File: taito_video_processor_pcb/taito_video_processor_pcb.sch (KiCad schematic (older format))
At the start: 342 parts, among them J1 14pin, J19 2pin, J2 14pin, J3 50pin, J6 50pin, Q1 2N3904, Q2 2N3904, Q3 2N3904, Q4 2N3904, Q5 2N3904, Q6 2N3904, Q7 2N3904, Q8 2N3905, SW1 SW_Push, U1 245_1, U10 4116, U100 LS00, U101 LS08, U102 LS10, U103 LS00, U104 157_1, U105 299_1, U106 299_1, U107 299_1, U108 299_1, U109 299_1, U11 4116, U110 299_1, U12 4116, U13 4116, U14 4116, U15 4116, U16 4116, U17 4116, U18 68A45, U19 86_2, U2 245_1, U20 86_1, U21 157_1, U22 LS32, U23 161_1, U24 LS04, U25 374_1, U26 4116, U27 4116, U28 4116, U29 4116, U3 2114, U30 4116, U31 4116, U32 4116, U33 4116, U34 LS374, U35 153_1, U36 LS74, U37 LS08, U38 74S113, U39 LS04, U4 2114, U40 7417, U41 4116, U42 4116, U43 4116, U44 4116, U45 4116, U46 4116, U47 4116, U48 4116, U49 LS32, U5 157_1, U50 86_3, U51 LS86, U52 153_1, U53 153_1, U54 153_1, U55 157_1, U56 2148_1, U57 2148_2, U58 7417, U59 4116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

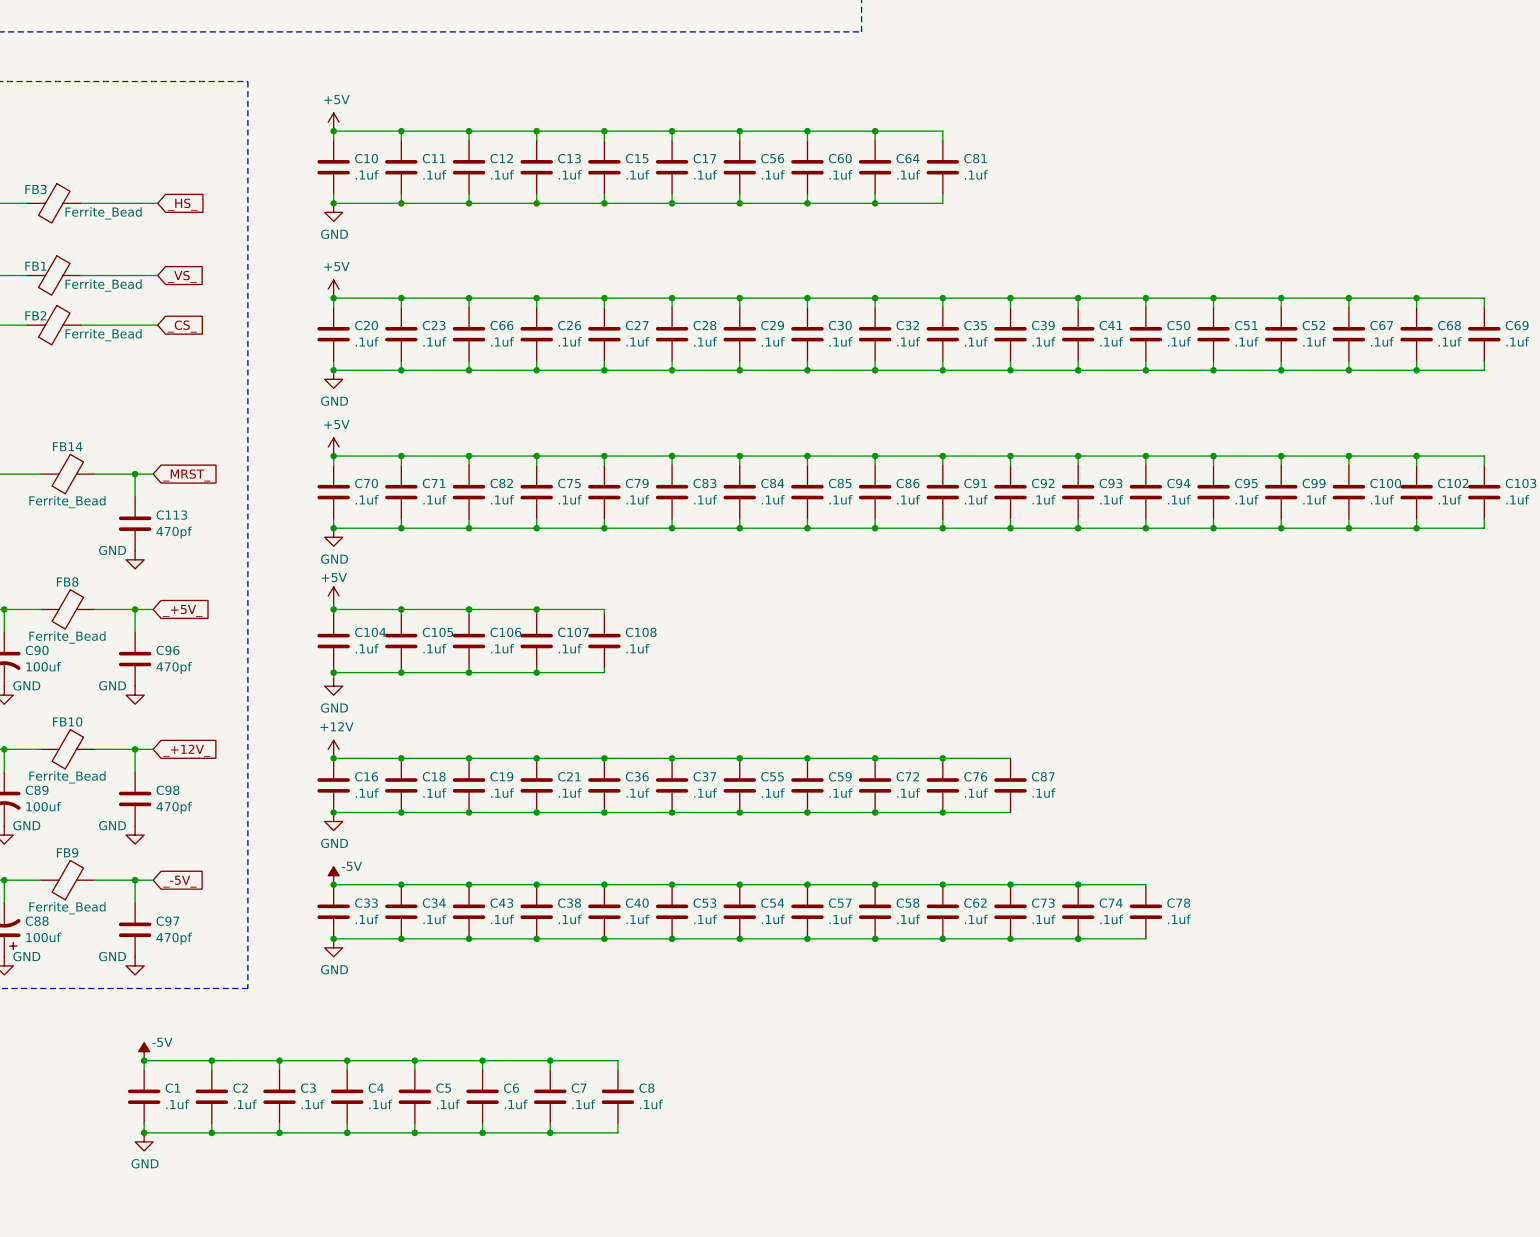
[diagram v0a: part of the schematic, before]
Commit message: Added traces
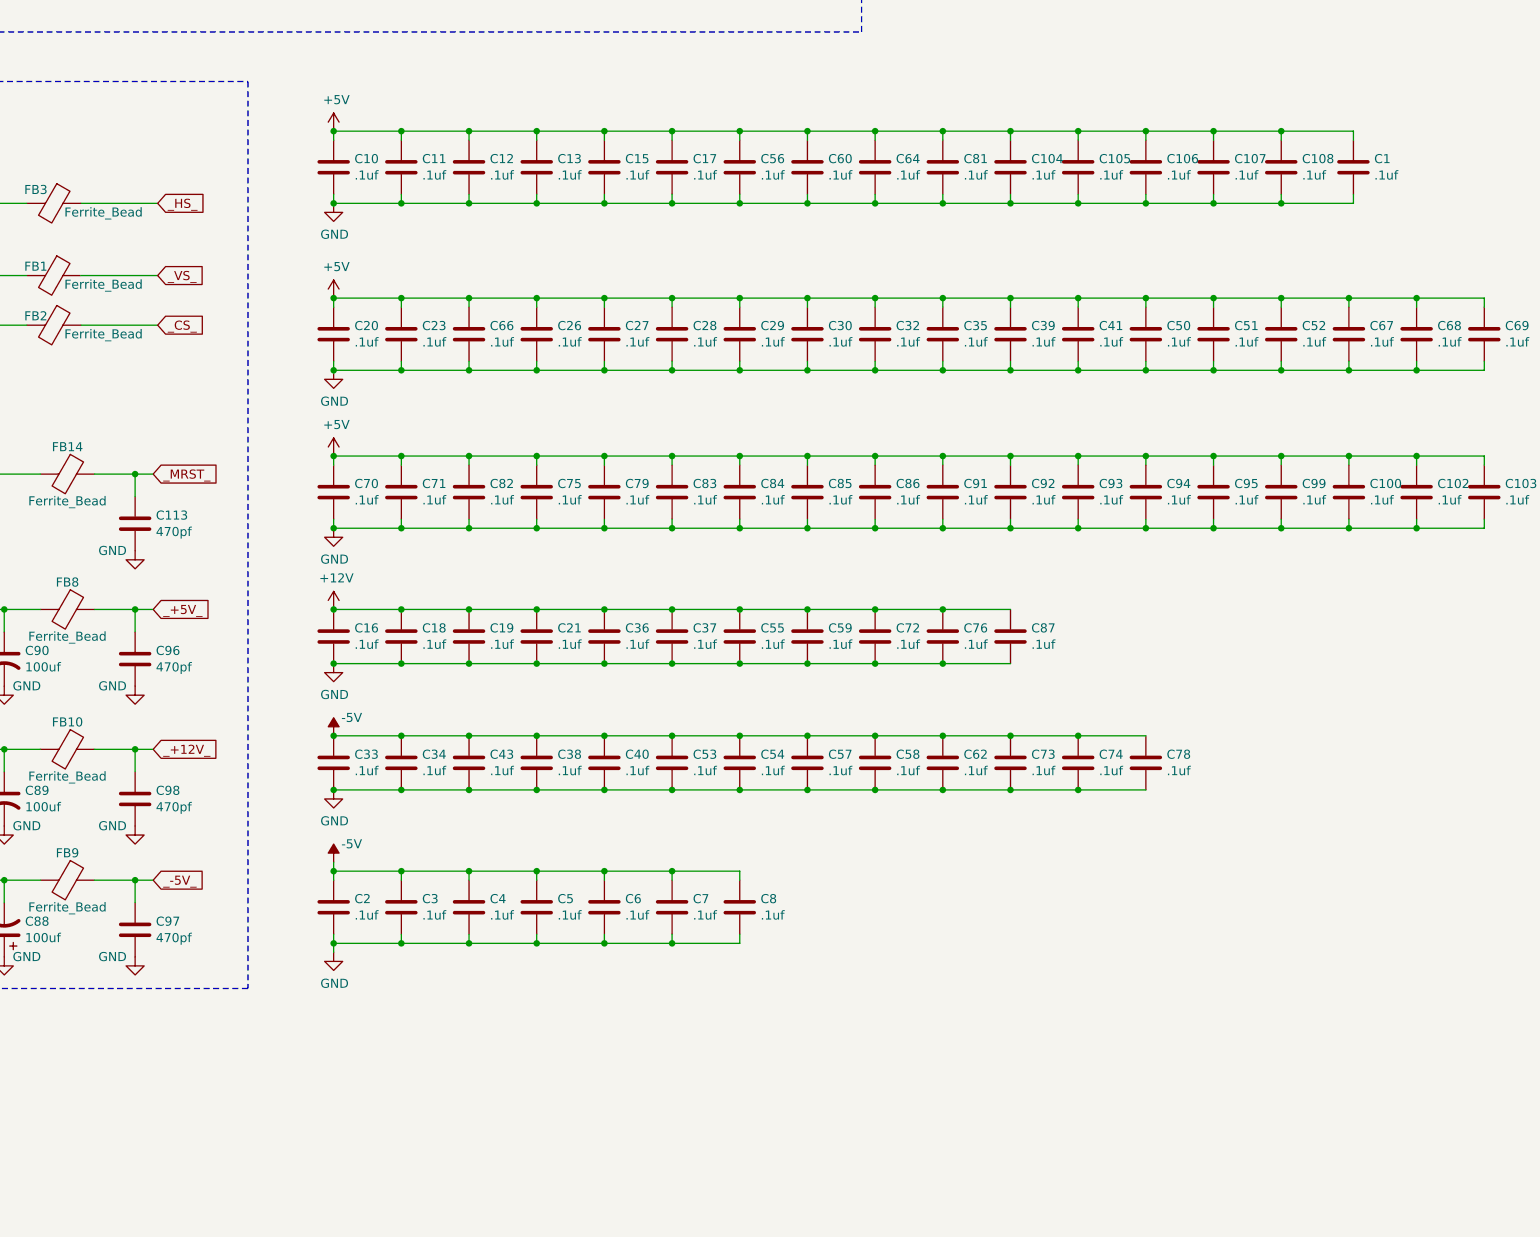
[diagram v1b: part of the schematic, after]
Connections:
- net +5V: now also C1.1
- net -5V: no longer C1.1
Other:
- moved on the sheet: C1, C104, C105, C106, C107, C108, C16, C18, C19, C2, C21, C3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

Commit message: Added more traces
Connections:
- net ~CAS1 is gone; now on net ~CAS: R9.1, RP1.2
- net +12V: now also C41.1
- net +5V: no longer C41.1
- net _VS: no longer R5.2
- net ~CAS: no longer R9.2, U25.19
- net at FB3.2, U40.2, U51.12: now also R5.2
- new net: R9.2, U25.19
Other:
- moved on the sheet: C41, C50, C51, C52, C67, C68, C69, R9
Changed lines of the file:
@@
 ~RAS
 Text GLabel 2425 1350 3    30   Input ~ 0
-~CAS1
+~CAS
 Text GLabel 2525 1350 3    30   Input ~ 0
 M6
@@
 Wire Wire Line
 	21900 6500 20225 6500
-Text GLabel 21900 6600 2    30   Input ~ 0
+Text GLabel 21450 6600 2    30   Input ~ 0
 ~CAS
 Wire Wire Line
-	21900 6600 20950 6600
-Wire Wire Line
 	22050 6000 22025 6000
 Wire Wire Line
@@
 Connection ~ 20775 17225
 Wire Wire Line
-	20775 17225 24275 17225
+	20775 17225 23900 17225
 Wire Wire Line
 	20900 18000 20600 18000
@@
 	23550 17125 23550 17625
 Connection ~ 23550 17625
-Wire Wire Line
-	23550 17625 23900 17625
-Wire Wire Line
-	23900 17125 23900 17625
-Connection ~ 23900 17625
-Wire Wire Line
-	23900 17625 24275 17625
 $Comp
 L power:+5V #PWR0325
@@
 L Device:R_US R9
 U 1 1 6BCCBBD6
-P 21225 6750
-F 0 "R9" V 21300 6750 50  0000 L CNN
-F 1 "?" V 21300 6625 50  0000 L CNN
-F 2 "taito_video_processor_pcb:GenericComp" V 21265 6740 50  0001 C CNN
-F 3 "~" H 21225 6750 50  0001 C CNN
-	1    21225 6750
+P 21225 6600
+F 0 "R9" V 21300 6600 50  0000 L CNN
+F 1 "?" V 21300 6475 50  0000 L CNN
+F 2 "taito_video_processor_pcb:GenericComp" V 21265 6590 50  0001 C CNN
+F 3 "~" H 21225 6600 50  0001 C CNN
+	1    21225 6600
 	0    1    1    0
 $EndComp
 Wire Wire Line
-	21075 6750 20950 6750
-Wire Wire Line
-	20950 6750 20950 6600
-Connection ~ 20950 6600
-Wire Wire Line
-	20950 6600 20225 6600
-Text GLabel 21375 6750 2    30   Input ~ 0
-~CAS1
+	21075 6600 20225 6600
 $Comp
 L Device:C C46
@@
 L Device:C C41
 U 1 1 7354F15C
-P 30100 17950
-F 0 "C41" H 30215 17996 50  0000 L CNN
-F 1 ".1uf" H 30215 17905 50  0000 L CNN
-F 2 "taito_video_processor_pcb:GenericComp" H 30138 17800 50  0001 C CNN
-F 3 "~" H 30100 17950 50  0001 C CNN
-	1    30100 17950
+P 30100 19625
+F 0 "C41" H 30215 19671 50  0000 L CNN
+F 1 ".1uf" H 30215 19580 50  0000 L CNN
+F 2 "taito_video_processor_pcb:GenericComp" H 30138 19475 50  0001 C CNN
+F 3 "~" H 30100 19625 50  0001 C CNN
+	1    30100 19625
 	1    0    0    -1
 $EndComp
@@
 L Device:C C50
 U 1 1 7833D507
+P 30100 17950
+F 0 "C50" H 30215 17996 50  0000 L CNN
+F 1 ".1uf" H 30215 17905 50  0000 L CNN
+F 2 "taito_video_processor_pcb:GenericComp" H 30138 17800 50  0001 C CNN
+F 3 "~" H 30100 17950 50  0001 C CNN
+	1    30100 17950
+	1    0    0    -1
+$EndComp
+$Comp
+L Device:C C51
+U 1 1 7833F111
 P 30475 17950
-F 0 "C50" H 30590 17996 50  0000 L CNN
+F 0 "C51" H 30590 17996 50  0000 L CNN
 F 1 ".1uf" H 30590 17905 50  0000 L CNN
 F 2 "taito_video_processor_pcb:GenericComp" H 30513 17800 50  0001 C CNN
@@
 	1    0    0    -1
 $EndComp
+Wire Wire Line
+	30475 17750 30475 17800
+Wire Wire Line
+	30475 18150 30475 18100
 $Comp
-L Device:C C51
-U 1 1 7833F111
+L Device:C C52
+U 1 1 7973627F
 P 30850 17950
-F 0 "C51" H 30965 17996 50  0000 L CNN
+F 0 "C52" H 30965 17996 50  0000 L CNN
 F 1 ".1uf" H 30965 17905 50  0000 L CNN
 F 2 "taito_video_processor_pcb:GenericComp" H 30888 17800 50  0001 C CNN
@@
 $EndComp
 Wire Wire Line
-	30100 17750 30475 17750
+	30475 17750 30850 17750
 Wire Wire Line
 	30850 17750 30850 17800
-Connection ~ 30100 17750
-Wire Wire Line
-	30100 18150 30475 18150
 Wire Wire Line
 	30850 18150 30850 18100
-Connection ~ 30100 18150
-Wire Wire Line
-	30475 17800 30475 17750
-Connection ~ 30475 17750
-Wire Wire Line
-	30475 17750 30850 17750
-Wire Wire Line
-	30475 18100 30475 18150
-Connection ~ 30475 18150
 Wire Wire Line
 	30475 18150 30850 18150
 $Comp
-L Device:C C52
-U 1 1 7973627F
-P 31225 17950
-F 0 "C52" H 31340 17996 50  0000 L CNN
-F 1 ".1uf" H 31340 17905 50  0000 L CNN
-F 2 "taito_video_processor_pcb:GenericComp" H 31263 17800 50  0001 C CNN
-F 3 "~" H 31225 17950 50  0001 C CNN
-	1    31225 17950
-	1    0    0    -1
-$EndComp
-Wire Wire Line
-	30850 17750 31225 17750
-Wire Wire Line
-	31225 17750 31225 17800
-Connection ~ 30850 17750
-Wire Wire Line
-	31225 18150 31225 18100
-Wire Wire Line
-	30850 18150 31225 18150
-Connection ~ 30850 18150
-$Comp
 L Device:C C55
 U 1 1 7B7550BD
@@
 L Device:C C67
 U 1 1 8C2D9D09
+P 31225 17950
+F 0 "C67" H 31340 17996 50  0000 L CNN
+F 1 ".1uf" H 31340 17905 50  0000 L CNN
+F 2 "taito_video_processor_pcb:GenericComp" H 31263 17800 50  0001 C CNN
+F 3 "~" H 31225 17950 50  0001 C CNN
+	1    31225 17950
+	1    0    0    -1
+$EndComp
+$Comp
+L Device:C C68
+U 1 1 8C2D9FBE
 P 31600 17950
-F 0 "C67" H 31715 17996 50  0000 L CNN
+F 0 "C68" H 31715 17996 50  0000 L CNN
 F 1 ".1uf" H 31715 17905 50  0000 L CNN
 F 2 "taito_video_processor_pcb:GenericComp" H 31638 17800 50  0001 C CNN
@@
 $EndComp
 $Comp
-L Device:C C68
-U 1 1 8C2D9FBE
+L Device:C C69
+U 1 1 8C2DA35B
 P 31975 17950
-F 0 "C68" H 32090 17996 50  0000 L CNN
+F 0 "C69" H 32090 17996 50  0000 L CNN
 F 1 ".1uf" H 32090 17905 50  0000 L CNN
 F 2 "taito_video_processor_pcb:GenericComp" H 32013 17800 50  0001 C CNN
@@
 $EndComp
 $Comp
-L Device:C C69
-U 1 1 8C2DA35B
-P 32350 17950
-F 0 "C69" H 32465 17996 50  0000 L CNN
-F 1 ".1uf" H 32465 17905 50  0000 L CNN
-F 2 "taito_video_processor_pcb:GenericComp" H 32388 17800 50  0001 C CNN
-F 3 "~" H 32350 17950 50  0001 C CNN
-	1    32350 17950
-	1    0    0    -1
-$EndComp
-$Comp
 L power:+5V #PWR0364
 U 1 1 8CB5A9D7
@@
 $EndComp
 Wire Wire Line
-	32350 17750 32350 17800
+	31975 17750 31975 17800
 Wire Wire Line
-	31225 18150 31600 18150
+	30850 18150 31225 18150
 Wire Wire Line
-	32350 18150 32350 18100
-Connection ~ 31225 18150
+	31975 18150 31975 18100
+Connection ~ 30850 18150
 Wire Wire Line
-	31225 17750 31600 17750
+	30850 17750 31225 17750
+Connection ~ 30850 17750
+Wire Wire Line
+	31225 17800 31225 17750
 Connection ~ 31225 17750
 Wire Wire Line
+	31225 17750 31600 17750
+Wire Wire Line
 	31600 17800 31600 17750
 Connection ~ 31600 17750
@@
 	31600 17750 31975 17750
 Wire Wire Line
-	31975 17800 31975 17750
-Connection ~ 31975 17750
-Wire Wire Line
-	31975 17750 32350 17750
-Wire Wire Line
-	31975 18100 31975 18150
-Connection ~ 31975 18150
-Wire Wire Line
-	31975 18150 32350 18150
-Wire Wire Line
 	31600 18100 31600 18150
 Connection ~ 31600 18150
 Wire Wire Line
 	31600 18150 31975 18150
+Wire Wire Line
+	31225 18100 31225 18150
+Connection ~ 31225 18150
+Wire Wire Line
+	31225 18150 31600 18150
 $Comp
 L Device:C C72
@@
 Connection ~ 29725 17225
 Connection ~ 29350 17225
+Wire Wire Line
+	21375 6600 21450 6600
+Wire Wire Line
+	23550 17625 24275 17625
+Wire Wire Line
+	23900 17125 23900 17225
+Connection ~ 23900 17225
+Wire Wire Line
+	23900 17225 24275 17225
+Wire Wire Line
+	30100 19475 29725 19475
+Connection ~ 29725 19475
+Wire Wire Line
+	29725 19775 30100 19775
+Connection ~ 29725 19775
+Wire Wire Line
+	30475 17750 30100 17750
+Connection ~ 30475 17750
+Connection ~ 30100 17750
+Wire Wire Line
+	30475 18150 30100 18150
+Connection ~ 30475 18150
+Connection ~ 30100 18150
 $EndSCHEMATC

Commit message: 1285 signal left to connect
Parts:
- removed unit 2 of U67
- removed unit 1 of U67
- added unit 1 of U67
- added unit 2 of U67
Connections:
- net +5V: now also U67.14 (VCC)
- net GND: now also U67.7 (GND)
- net ~EVEN1: now also U67.2
- net ~ODD1: now also U67.5
- net ~VEW: now also U67.1, U67.4
- net at R36.2: now also U67.3
- net at R21.2: now also U67.6
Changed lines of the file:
@@
 $Comp
 L Asteroids:LS32 U67
-U 2 1 82B14B16
-P 10525 19450
-F 0 "U67" H 10525 19475 50  0000 C CNN
-F 1 "LS32" H 10525 19400 50  0000 C CNN
-F 2 "Star_Wars_Vector_PCB:DIP14" H 10525 19450 50  0001 C CNN
-F 3 "" H 10525 19450 50  0001 C CNN
-	2    10525 19450
-	1    0    0    -1
-$EndComp
-$Comp
-L Asteroids:LS32 U67
 U 3 1 82B14B1C
 P 10550 15150
@@
 $Comp
 L Asteroids:LS32 U67
-U 1 2 82B14CE6
-P 10550 14625
-F 0 "U67" H 10500 14675 50  0000 L CNN
-F 1 "LS32" H 10500 14600 50  0000 L CNN
-F 2 "Star_Wars_Vector_PCB:DIP14" H 10550 14625 50  0001 C CNN
-F 3 "" H 10550 14625 50  0001 C CNN
-	1    10550 14625
-	1    0    0    -1
-$EndComp
-$Comp
-L power:+5V #PWR0291
-U 1 1 82B14CEC
-P 10425 14425
-F 0 "#PWR0291" H 10425 14275 50  0001 C CNN
-F 1 "+5V" H 10550 14500 50  0000 C CNN
-F 2 "" H 10425 14425 50  0001 C CNN
-F 3 "" H 10425 14425 50  0001 C CNN
-	1    10425 14425
-	1    0    0    -1
-$EndComp
-$Comp
-L power:GND #PWR0292
-U 1 1 82B14CF2
-P 10425 14825
-F 0 "#PWR0292" H 10425 14575 50  0001 C CNN
-F 1 "GND" H 10575 14750 50  0000 C CNN
-F 2 "" H 10425 14825 50  0001 C CNN
-F 3 "" H 10425 14825 50  0001 C CNN
-	1    10425 14825
-	1    0    0    -1
-$EndComp
-$Comp
-L Asteroids:LS32 U67
 U 4 2 82B14CF8
 P 10500 20100
@@
 Connection ~ 30475 18150
 Connection ~ 30100 18150
+$Comp
+L Star_Wars_Vector_PCB:LS32 U67
+U 1 1 6E790DF4
+P 10525 19450
+F 0 "U67" H 10475 19500 50  0000 L CNN
+F 1 "LS32" H 10475 19400 50  0000 L CNN
+F 2 "" H 10525 19450 50  0001 C CNN
+F 3 "" H 10525 19450 50  0001 C CNN
+	1    10525 19450
+	1    0    0    -1
+$EndComp
+$Comp
+L power:GND #PWR?
+U 1 1 6E792899
+P 10400 19650
+F 0 "#PWR?" H 10400 19400 50  0001 C CNN
+F 1 "GND" H 10550 19600 50  0000 C CNN
+F 2 "" H 10400 19650 50  0001 C CNN
+F 3 "" H 10400 19650 50  0001 C CNN
+	1    10400 19650
+	1    0    0    -1
+$EndComp
+$Comp
+L power:+5V #PWR?
+U 1 1 6E793344
+P 10400 19250
+F 0 "#PWR?" H 10400 19100 50  0001 C CNN
+F 1 "+5V" H 10500 19325 50  0000 C CNN
+F 2 "" H 10400 19250 50  0001 C CNN
+F 3 "" H 10400 19250 50  0001 C CNN
+	1    10400 19250
+	1    0    0    -1
+$EndComp
+$Comp
+L Star_Wars_Vector_PCB:LS32 U67
+U 2 2 6EC2487B
+P 10550 14625
+F 0 "U67" H 10550 14650 50  0000 C CNN
+F 1 "LS32" H 10550 14575 50  0000 C CNN
+F 2 "" H 10550 14625 50  0001 C CNN
+F 3 "" H 10550 14625 50  0001 C CNN
+	2    10550 14625
+	1    0    0    -1
+$EndComp
 $EndSCHEMATC

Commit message: 938 disconnected signals remain
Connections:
- net ~EVEN1: now also U67.10, U67.5; no longer U67.13, U67.2
- net ~MRST: no longer RP5.2
- net ~ODD1: now also U67.13, U67.2; no longer U67.10, U67.5
- net PU1: now reaches U100.12, U101.3
- net PU1: now also RP5.2
- net at U67.3: now also R21.2; no longer R36.2
- net at U67.6: now also R36.2; no longer R21.2
- net at U79.1 (~OE): now also U67.11; no longer U67.8
- net at U80.1 (~OE): now also U67.8; no longer U67.11
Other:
- moved on the sheet: U67B, U67D
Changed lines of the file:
@@
 	3925 1300 3925 1350
 Text GLabel 7225 1350 3    30   Input ~ 0
-~MRST
+PU1
 Wire Wire Line
 	7225 1300 7225 1350
@@
 $EndComp
 Wire Wire Line
-	13300 2400 12825 2400
+	13300 2400 13150 2400
 $Comp
 L Asteroids:LS10 U102
@@
 $Comp
 L Asteroids:LS32 U67
-U 3 1 82B14B1C
-P 10550 15150
-F 0 "U67" H 10550 15125 50  0000 C CNN
-F 1 "LS32" H 10550 15200 50  0000 C CNN
-F 2 "Star_Wars_Vector_PCB:DIP14" H 10550 15150 50  0001 C CNN
-F 3 "" H 10550 15150 50  0001 C CNN
-	3    10550 15150
+U 3 2 82B14B1C
+P 10500 20100
+F 0 "U67" H 10500 20075 50  0000 C CNN
+F 1 "LS32" H 10500 20150 50  0000 C CNN
+F 2 "Star_Wars_Vector_PCB:DIP14" H 10500 20100 50  0001 C CNN
+F 3 "" H 10500 20100 50  0001 C CNN
+	3    10500 20100
 	1    0    0    1
 $EndComp
@@
 L Asteroids:LS32 U67
 U 4 2 82B14CF8
-P 10500 20100
-F 0 "U67" H 10475 20150 50  0000 C CNN
-F 1 "LS32" H 10475 20075 50  0000 C CNN
-F 2 "Star_Wars_Vector_PCB:DIP14" H 10500 20100 50  0001 C CNN
-F 3 "" H 10500 20100 50  0001 C CNN
-	4    10500 20100
+P 10550 15150
+F 0 "U67" H 10525 15200 50  0000 C CNN
+F 1 "LS32" H 10525 15125 50  0000 C CNN
+F 2 "Star_Wars_Vector_PCB:DIP14" H 10550 15150 50  0001 C CNN
+F 3 "" H 10550 15150 50  0001 C CNN
+	4    10550 15150
 	1    0    0    1
 $EndComp
@@
 $Comp
 L Star_Wars_Vector_PCB:LS32 U67
-U 1 1 6E790DF4
-P 10525 19450
-F 0 "U67" H 10475 19500 50  0000 L CNN
-F 1 "LS32" H 10475 19400 50  0000 L CNN
-F 2 "" H 10525 19450 50  0001 C CNN
-F 3 "" H 10525 19450 50  0001 C CNN
-	1    10525 19450
+U 1 2 6E790DF4
+P 10550 14625
+F 0 "U67" H 10500 14675 50  0000 L CNN
+F 1 "LS32" H 10500 14575 50  0000 L CNN
+F 2 "" H 10550 14625 50  0001 C CNN
+F 3 "" H 10550 14625 50  0001 C CNN
+	1    10550 14625
 	1    0    0    -1
 $EndComp
 $Comp
-L power:GND #PWR?
+L power:GND #PWR0291
 U 1 1 6E792899
-P 10400 19650
-F 0 "#PWR?" H 10400 19400 50  0001 C CNN
-F 1 "GND" H 10550 19600 50  0000 C CNN
-F 2 "" H 10400 19650 50  0001 C CNN
-F 3 "" H 10400 19650 50  0001 C CNN
-	1    10400 19650
+P 10425 14825
+F 0 "#PWR0291" H 10425 14575 50  0001 C CNN
+F 1 "GND" H 10575 14775 50  0000 C CNN
+F 2 "" H 10425 14825 50  0001 C CNN
+F 3 "" H 10425 14825 50  0001 C CNN
+	1    10425 14825
 	1    0    0    -1
 $EndComp
 $Comp
-L power:+5V #PWR?
+L power:+5V #PWR0292
 U 1 1 6E793344
-P 10400 19250
-F 0 "#PWR?" H 10400 19100 50  0001 C CNN
-F 1 "+5V" H 10500 19325 50  0000 C CNN
-F 2 "" H 10400 19250 50  0001 C CNN
-F 3 "" H 10400 19250 50  0001 C CNN
-	1    10400 19250
+P 10425 14425
+F 0 "#PWR0292" H 10425 14275 50  0001 C CNN
+F 1 "+5V" H 10525 14500 50  0000 C CNN
+F 2 "" H 10425 14425 50  0001 C CNN
+F 3 "" H 10425 14425 50  0001 C CNN
+	1    10425 14425
 	1    0    0    -1
 $EndComp
@@
 L Star_Wars_Vector_PCB:LS32 U67
 U 2 2 6EC2487B
-P 10550 14625
-F 0 "U67" H 10550 14650 50  0000 C CNN
-F 1 "LS32" H 10550 14575 50  0000 C CNN
-F 2 "" H 10550 14625 50  0001 C CNN
-F 3 "" H 10550 14625 50  0001 C CNN
-	2    10550 14625
+P 10525 19450
+F 0 "U67" H 10525 19475 50  0000 C CNN
+F 1 "LS32" H 10525 19400 50  0000 C CNN
+F 2 "" H 10525 19450 50  0001 C CNN
+F 3 "" H 10525 19450 50  0001 C CNN
+	2    10525 19450
 	1    0    0    -1
 $EndComp
+Text GLabel 13075 2275 0    50   Input ~ 0
+PU1
+Wire Wire Line
+	13075 2275 13150 2275
+Wire Wire Line
+	13150 2275 13150 2400
+Connection ~ 13150 2400
+Wire Wire Line
+	13150 2400 12825 2400
 $EndSCHEMATC

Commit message: 694 disconnected signals remain
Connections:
- net ~E: now also J6.25
- net ~QX: no longer J6.25
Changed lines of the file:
@@
 Q
 Text GLabel 31375 13325 0    30   Input ~ 0
-~QX
+~E
 Wire Wire Line
 	31375 13625 31175 13625
